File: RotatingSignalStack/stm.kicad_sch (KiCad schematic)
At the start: 16 parts, among them IC2 STM32H562RIT6, SW1 SW_Push, SW2 Boot Switch

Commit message: Minimal schematic
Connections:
- net STM_CLK_IN: now also IC2.5 (PH0-OSC_IN); no longer IC2.3 (PC14-OSC32_IN)
- no-connect marks 0 -> 29
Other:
- moved on the sheet: C13, C19, C20, C21, C30, C31, C32, C33, C34, C35

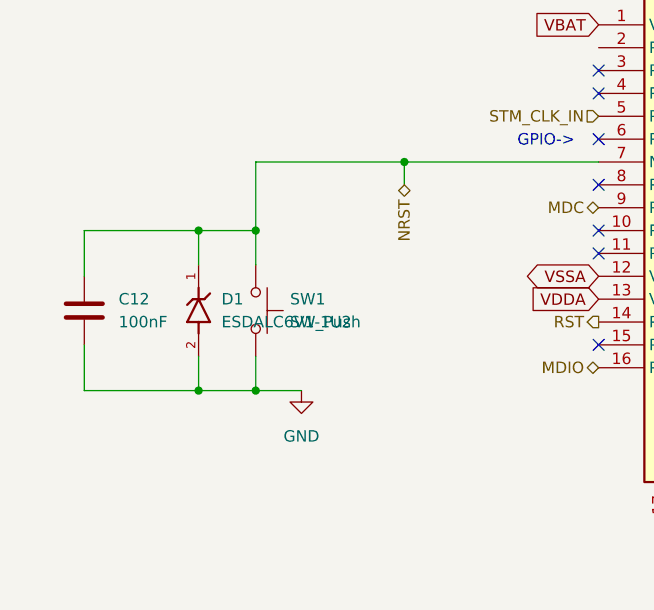
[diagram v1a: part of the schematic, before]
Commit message: Added ethernel ESD protection
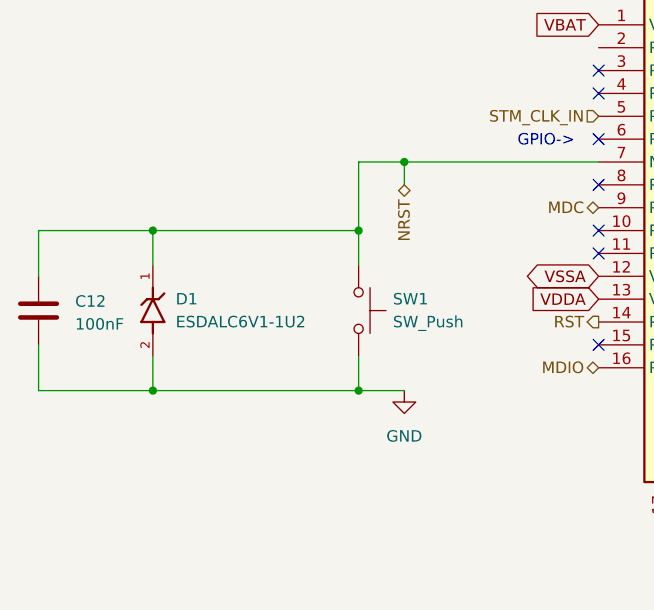
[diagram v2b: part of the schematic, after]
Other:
- moved on the sheet: C12, D1, SW1
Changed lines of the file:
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@@
 	)
 	(junction
-		(at 41.91 110.49)
+		(at 53.34 110.49)
 		(diameter 0)
 		(color 0 0 0 0)
 	)
 	(junction
-		(at 41.91 128.27)
+		(at 53.34 128.27)
 		(diameter 0)
 		(color 0 0 0 0)
@@
 	)
 	(junction
-		(at 35.56 110.49)
+		(at 30.48 110.49)
 		(diameter 0)
 		(color 0 0 0 0)
@@
 	)
 	(junction
-		(at 35.56 128.27)
+		(at 30.48 128.27)
 		(diameter 0)
 		(color 0 0 0 0)
@@
 	(wire
 		(pts
-			(xy 41.91 110.49) (xy 41.91 114.3)
+			(xy 53.34 110.49) (xy 53.34 114.3)
 		)
 		(stroke
@@
 	(wire
 		(pts
-			(xy 35.56 110.49) (xy 41.91 110.49)
+			(xy 30.48 110.49) (xy 53.34 110.49)
 		)
 		(stroke
@@
 	(wire
 		(pts
-			(xy 41.91 128.27) (xy 35.56 128.27)
+			(xy 53.34 128.27) (xy 30.48 128.27)
 		)
 		(stroke
@@
 	(wire
 		(pts
-			(xy 35.56 124.46) (xy 35.56 128.27)
+			(xy 30.48 124.46) (xy 30.48 128.27)
 		)
 		(stroke
@@
 	(wire
 		(pts
-			(xy 41.91 124.46) (xy 41.91 128.27)
+			(xy 53.34 124.46) (xy 53.34 128.27)
 		)
 		(stroke
@@
 	(wire
 		(pts
-			(xy 35.56 110.49) (xy 35.56 114.3)
+			(xy 30.48 110.49) (xy 30.48 114.3)
 		)
 		(stroke
@@
 	(wire
 		(pts
-			(xy 22.86 128.27) (xy 22.86 123.19)
-		)
-		(stroke
-			(width 0)
-			(type default)
-		)
-	)
-	(wire
-		(pts
 			(xy 58.42 102.87) (xy 58.42 105.41)
 		)
@@
 	(wire
 		(pts
-			(xy 22.86 115.57) (xy 22.86 110.49)
+			(xy 251.46 33.02) (xy 252.73 33.02)
 		)
 		(stroke
@@
 	(wire
 		(pts
-			(xy 35.56 128.27) (xy 22.86 128.27)
+			(xy 251.46 29.21) (xy 252.73 29.21)
 		)
 		(stroke
@@
 	(wire
 		(pts
-			(xy 251.46 33.02) (xy 252.73 33.02)
+			(xy 252.73 68.58) (xy 267.97 68.58)
 		)
 		(stroke
@@
 	(wire
 		(pts
-			(xy 251.46 29.21) (xy 252.73 29.21)
+			(xy 222.25 21.59) (xy 222.25 25.4)
 		)
 		(stroke
@@
 	(wire
 		(pts
-			(xy 252.73 68.58) (xy 267.97 68.58)
+			(xy 218.44 33.02) (xy 222.25 33.02)
 		)
 		(stroke
@@
 	(wire
 		(pts
-			(xy 222.25 21.59) (xy 222.25 25.4)
+			(xy 58.42 128.27) (xy 53.34 128.27)
 		)
 		(stroke
@@
 	(wire
 		(pts
-			(xy 22.86 110.49) (xy 35.56 110.49)
+			(xy 252.73 33.02) (xy 252.73 35.56)
 		)
 		(stroke
@@
 	(wire
 		(pts
-			(xy 218.44 33.02) (xy 222.25 33.02)
+			(xy 17.78 110.49) (xy 30.48 110.49)
 		)
 		(stroke
@@
 	(wire
 		(pts
-			(xy 46.99 128.27) (xy 41.91 128.27)
+			(xy 252.73 91.44) (xy 252.73 86.36)
 		)
 		(stroke
@@
 	(wire
 		(pts
-			(xy 252.73 33.02) (xy 252.73 35.56)
+			(xy 252.73 25.4) (xy 252.73 29.21)
 		)
 		(stroke
@@
 	(wire
 		(pts
-			(xy 252.73 91.44) (xy 252.73 86.36)
+			(xy 196.85 25.4) (xy 200.66 25.4)
 		)
 		(stroke
@@
 	(wire
 		(pts
-			(xy 252.73 25.4) (xy 252.73 29.21)
+			(xy 218.44 29.21) (xy 222.25 29.21)
 		)
 		(stroke
@@
 	(wire
 		(pts
-			(xy 196.85 25.4) (xy 200.66 25.4)
+			(xy 17.78 110.49) (xy 17.78 115.57)
 		)
 		(stroke
@@
 	(wire
 		(pts
-			(xy 218.44 29.21) (xy 222.25 29.21)
+			(xy 222.25 25.4) (xy 222.25 29.21)
 		)
 		(stroke
@@
 	(wire
 		(pts
-			(xy 222.25 25.4) (xy 222.25 29.21)
+			(xy 17.78 123.19) (xy 17.78 128.27)
 		)
 		(stroke
@@
 	(wire
 		(pts
-			(xy 41.91 102.87) (xy 41.91 110.49)
+			(xy 53.34 102.87) (xy 53.34 110.49)
+		)
+		(stroke
+			(width 0)
+			(type default)
+		)
+	)
+	(wire
+		(pts
+			(xy 17.78 128.27) (xy 30.48 128.27)
 		)
 		(stroke
@@
 	(wire
 		(pts
-			(xy 58.42 102.87) (xy 41.91 102.87)
+			(xy 53.34 102.87) (xy 58.42 102.87)
 		)
 		(stroke
@@
 	(symbol
 		(lib_id "Switch:SW_Push")
-		(at 41.91 119.38 270)
+		(at 53.34 119.38 270)
 		(unit 1)
 		(exclude_from_sim no)
@@
 		(fields_autoplaced yes)
 		(property "Reference" "SW1"
-			(at 45.72 118.1099 90)
+			(at 57.15 118.1099 90)
 			(effects
 				(font
@@
 		)
 		(property "Value" "SW_Push"
-			(at 45.72 120.6499 90)
+			(at 57.15 120.6499 90)
 			(effects
 				(font
@@
 		)
 		(property "Footprint" ""
-			(at 46.99 119.38 0)
+			(at 58.42 119.38 0)
 			(effects
 				(font
@@
 		)
 		(property "Datasheet" "~"
-			(at 46.99 119.38 0)
+			(at 58.42 119.38 0)
 			(effects
 				(font
@@
 		)
 		(property "Description" "Push button switch, generic, two pins"
-			(at 41.91 119.38 0)
+			(at 53.34 119.38 0)
 			(effects
 				(font
@@
 	(symbol
 		(lib_id "ESDALC6V1-1U2:ESDALC6V1-1U2")
-		(at 35.56 119.38 90)
+		(at 30.48 119.38 90)
 		(unit 1)
 		(exclude_from_sim no)
@@
 		(fields_autoplaced yes)
 		(property "Reference" "D1"
-			(at 38.1 118.1099 90)
+			(at 33.02 118.1099 90)
 			(effects
 				(font
@@
 		)
 		(property "Value" "ESDALC6V1-1U2"
-			(at 38.1 120.6499 90)
+			(at 33.02 120.6499 90)
 			(effects
 				(font
@@
 		)
 		(property "Footprint" "ESDALC6V1-1U2:DIODE_ESDALC6V1-1U2"
-			(at 35.56 119.38 0)
+			(at 30.48 119.38 0)
 			(effects
 				(font
@@
 		)
 		(property "Datasheet" ""
-			(at 35.56 119.38 0)
+			(at 30.48 119.38 0)
 			(effects
 				(font
@@
 		)
 		(property "Description" ""
-			(at 35.56 119.38 0)
+			(at 30.48 119.38 0)
 			(effects
 				(font
@@
 		)
 		(property "PARTREV" "3"
-			(at 35.56 119.38 0)
+			(at 30.48 119.38 0)
 			(effects
 				(font
@@
 		)
 		(property "STANDARD" "Manufacturer Recommendations"
-			(at 35.56 119.38 0)
+			(at 30.48 119.38 0)
 			(effects
 				(font
@@
 		)
 		(property "MAXIMUM_PACKAGE_HEIGHT" "0.33mm"
-			(at 35.56 119.38 0)
+			(at 30.48 119.38 0)
 			(effects
 				(font
@@
 		)
 		(property "MANUFACTURER" "STMicroelectronics"
-			(at 35.56 119.38 0)
+			(at 30.48 119.38 0)
 			(effects
 				(font
@@
 	(symbol
 		(lib_id "Device:C")
-		(at 22.86 119.38 0)
+		(at 17.78 119.38 0)
 		(unit 1)
 		(exclude_from_sim no)
@@
 		(on_board yes)
 		(dnp no)
-		(fields_autoplaced yes)
 		(property "Reference" "C12"
-			(at 26.67 118.1099 0)
+			(at 21.844 118.364 0)
 			(effects
 				(font
@@
 		)
 		(property "Value" "100nF"
-			(at 26.67 120.6499 0)
+			(at 21.844 120.904 0)
 			(effects
 				(font
@@
 		)
 		(property "Footprint" ""
-			(at 23.8252 123.19 0)
+			(at 18.7452 123.19 0)
 			(effects
 				(font
@@
 		)
 		(property "Datasheet" "~"
-			(at 22.86 119.38 0)
+			(at 17.78 119.38 0)
 			(effects
 				(font
@@
 		)
 		(property "Description" "Unpolarized capacitor"
-			(at 22.86 119.38 0)
+			(at 17.78 119.38 0)
 			(effects
 				(font
@@
 	(symbol
 		(lib_id "power:GND")
-		(at 46.99 128.27 0)
+		(at 58.42 128.27 0)
 		(unit 1)
 		(exclude_from_sim no)
@@
 		(fields_autoplaced yes)
 		(property "Reference" "#PWR034"
-			(at 46.99 134.62 0)
+			(at 58.42 134.62 0)
 			(effects
 				(font
@@
 		)
 		(property "Value" "GND"
-			(at 46.99 133.35 0)
+			(at 58.42 133.35 0)
 			(effects
 				(font
@@
 		)
 		(property "Footprint" ""
-			(at 46.99 128.27 0)
+			(at 58.42 128.27 0)
 			(effects
 				(font
@@
 		)
 		(property "Datasheet" ""
-			(at 46.99 128.27 0)
+			(at 58.42 128.27 0)
 			(effects
 				(font
@@
 		)
 		(property "Description" "Power symbol creates a global label with name \"GND\" , ground"
-			(at 46.99 128.27 0)
+			(at 58.42 128.27 0)
 			(effects
 				(font

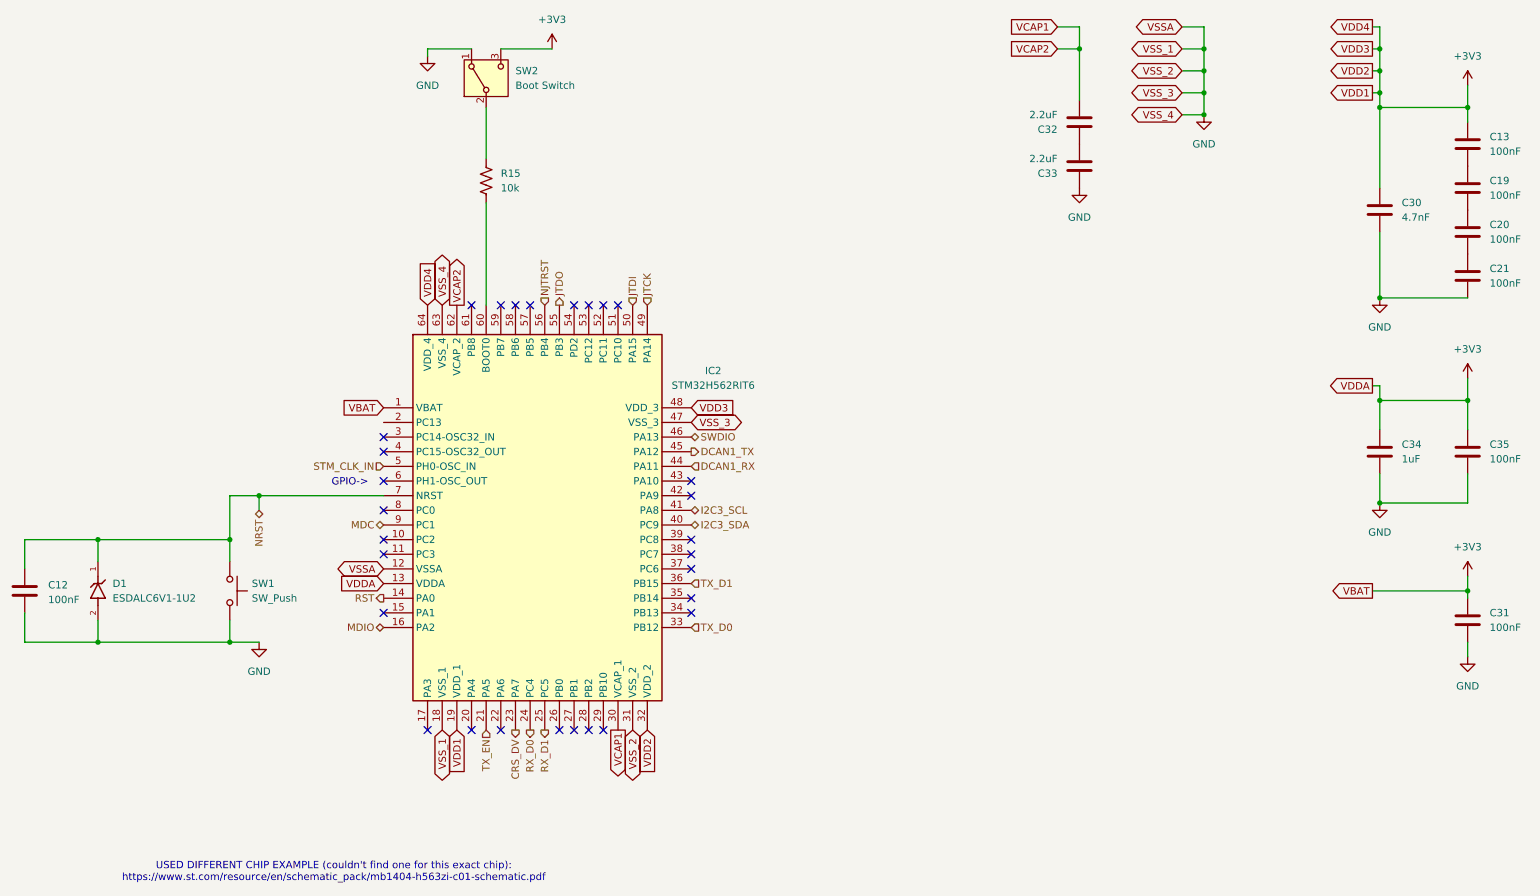
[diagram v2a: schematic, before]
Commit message: Added power LEDS
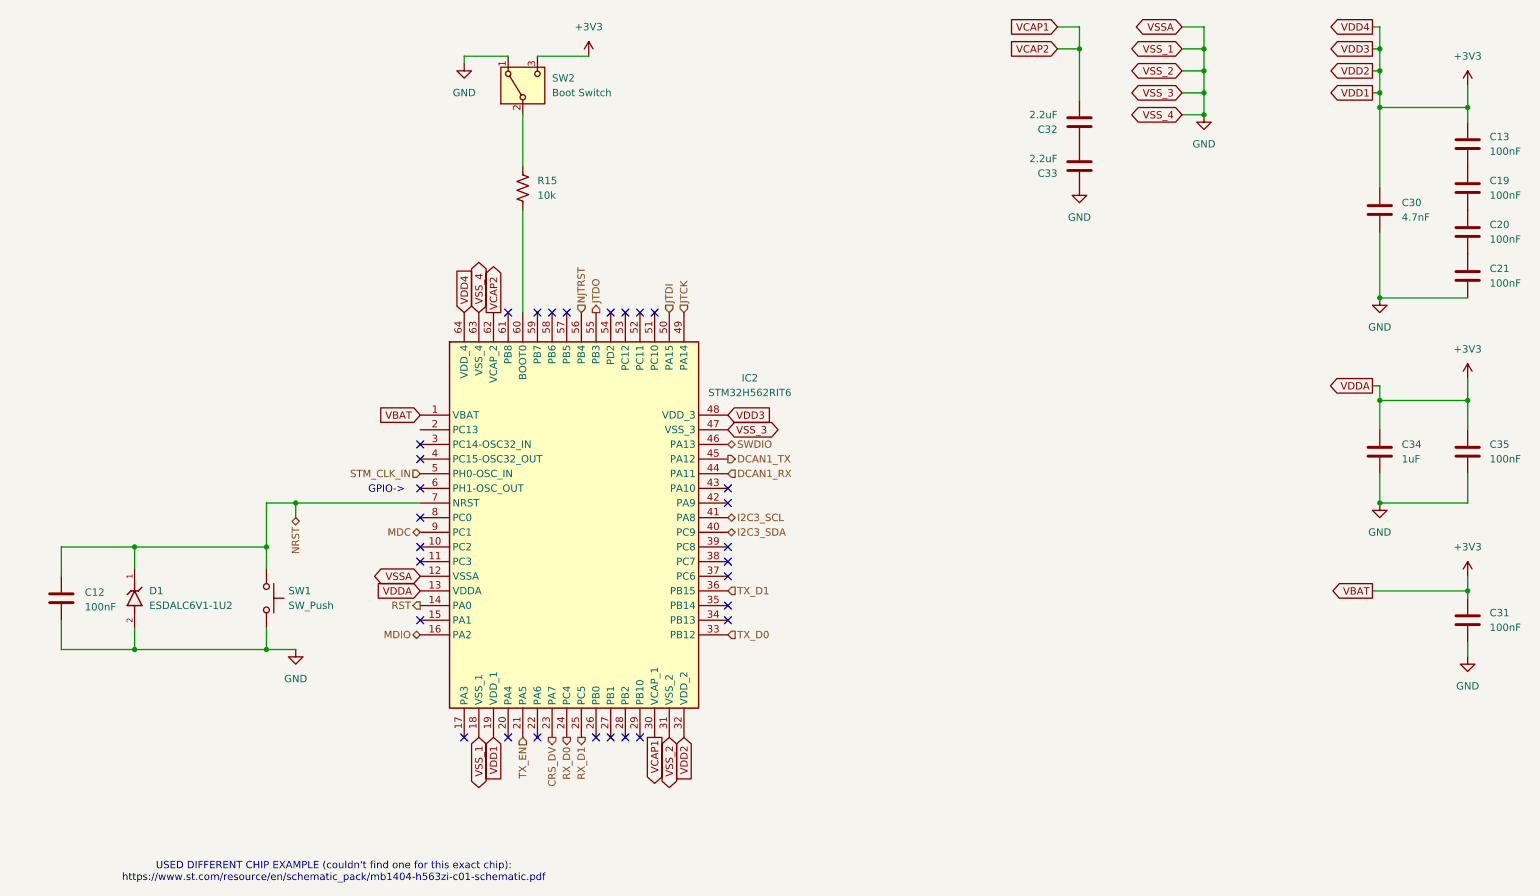
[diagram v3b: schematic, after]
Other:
- moved on the sheet: C12, D1, IC2, R15, SW1, SW2

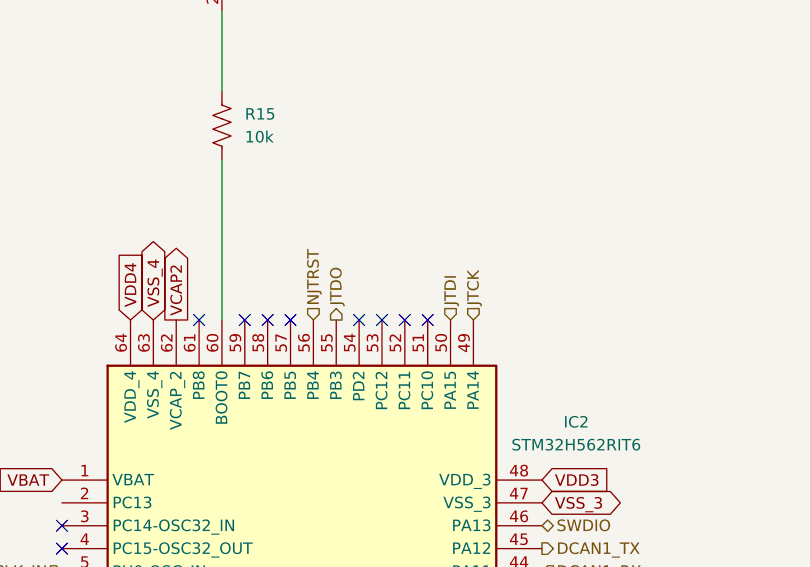
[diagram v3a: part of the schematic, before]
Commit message: Added buttons
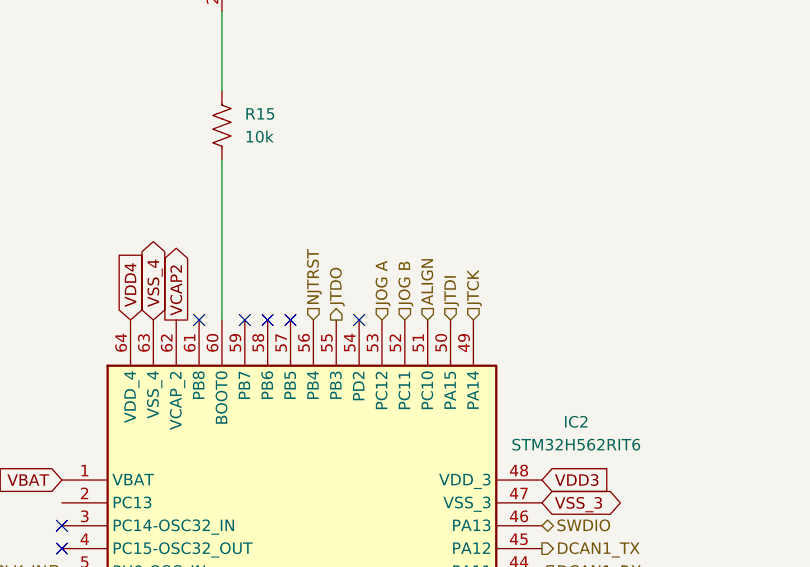
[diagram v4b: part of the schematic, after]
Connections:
- net ALIGN: now reaches IC2.51 (PC10)
- net JOG B: now reaches IC2.52 (PC11)
- net JOG A: now reaches IC2.53 (PC12)
- no-connect marks 29 -> 26
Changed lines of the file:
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@@
-	)
-	(no_connect
-		(at 127 71.12)
 	)
 	(no_connect
@@
 	)
 	(no_connect
-		(at 121.92 71.12)
-	)
-	(no_connect
 		(at 119.38 144.78)
 	)
@@
 	(no_connect
 		(at 139.7 101.6)
-	)
-	(no_connect
-		(at 124.46 71.12)
 	)
 	(no_connect
@@
 		)
 	)
+	(hierarchical_label "JOG B"
+		(shape input)
+		(at 124.46 71.12 90)
+		(effects
+			(font
+				(size 1.27 1.27)
+			)
+			(justify left)
+		)
+	)
 	(hierarchical_label "JTCK"
 		(shape input)
 		(at 132.08 71.12 90)
+		(effects
+			(font
+				(size 1.27 1.27)
+			)
+			(justify left)
+		)
+	)
+	(hierarchical_label "JOG A"
+		(shape input)
+		(at 121.92 71.12 90)
 		(effects
 			(font
@@
 		)
 	)
+	(hierarchical_label "ALIGN"
+		(shape input)
+		(at 127 71.12 90)
+		(effects
+			(font
+				(size 1.27 1.27)
+			)
+			(justify left)
+		)
+	)

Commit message: Added everything
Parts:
- C12, C13, C19, C20, C21, C30, C31, C32, C33, C34, C35: footprint (none) -> Capacitor_SMD:C_0603_1608Metric_Pad1.08x0.95mm_HandSolder
- D7: renamed from D1; footprint ESDALC6V1-1U2:DIODE_ESDALC6V1-1U2 -> SignalStack:DIODE_ESDALC6V1-1U2
- IC2: footprint QFP50P1200X1200X160-64N -> SignalStack:STM32H562RIT6
- R15: footprint (none) -> Resistor_SMD:R_0603_1608Metric_Pad0.98x0.95mm_HandSolder
- SW1: footprint (none) -> Button_Switch_SMD:SW_SPST_TL3305A
- SW2: footprint Button_Switch_THT:SW_Slide_SPDT_Angled_CK_OS102011MA1Q -> Button_Switch_THT:SW_Slide_SPDT_Straight_CK_OS102011MS2Q
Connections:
- net JTCK renamed SWCLK
- net JTDI: no longer names the net of IC2.50 (PA15)
- net JTDO renamed SWO
- net NJTRST: no longer names the net of IC2.56 (PB4)
- no-connect marks 26 -> 28
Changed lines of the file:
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@@
 	)
 	(no_connect
+		(at 114.3 71.12)
+	)
+	(no_connect
 		(at 86.36 96.52)
 	)
 	(no_connect
+		(at 129.54 71.12)
+	)
+	(no_connect
 		(at 86.36 93.98)
 	)
@@
 	(wire
 		(pts
+			(xy 222.25 39.37) (xy 222.25 36.83)
+		)
+		(stroke
+			(width 0)
+			(type default)
+		)
+	)
+	(wire
+		(pts
 			(xy 36.83 111.76) (xy 59.69 111.76)
 		)
@@
 	(wire
 		(pts
-			(xy 59.69 129.54) (xy 36.83 129.54)
+			(xy 36.83 129.54) (xy 59.69 129.54)
 		)
 		(stroke
@@
 		)
 	)
-	(hierarchical_label "JTDI"
-		(shape input)
-		(at 129.54 71.12 90)
-		(effects
-			(font
-				(size 1.27 1.27)
-			)
-			(justify left)
-		)
-	)
-	(hierarchical_label "JTDO"
+	(hierarchical_label "SWO"
 		(shape output)
 		(at 116.84 71.12 90)
@@
 		)
 	)
-	(hierarchical_label "JTCK"
+	(hierarchical_label "SWCLK"
 		(shape input)
 		(at 132.08 71.12 90)
@@
 		)
 	)
-	(hierarchical_label "NJTRST"
-		(shape input)
-		(at 114.3 71.12 90)
-		(effects
-			(font
-				(size 1.27 1.27)
-			)
-			(justify left)
-		)
-	)
 	(hierarchical_label "RX_D1"
 		(shape output)
@@
 			)
 		)
-		(property "Footprint" ""
+		(property "Footprint" "Button_Switch_SMD:SW_SPST_TL3305A"
 			(at 64.77 120.65 0)
 			(effects
@@
 			)
 		)
-		(property "Footprint" ""
+		(property "Footprint" "Capacitor_SMD:C_0603_1608Metric_Pad1.08x0.95mm_HandSolder"
 			(at 268.9352 53.34 0)
 			(effects
@@
 		(dnp no)
 		(fields_autoplaced yes)
-		(property "Reference" "D1"
+		(property "Reference" "D7"
 			(at 39.37 119.3799 90)
 			(effects
@@
 			)
 		)
-		(property "Footprint" "ESDALC6V1-1U2:DIODE_ESDALC6V1-1U2"
+		(property "Footprint" "SignalStack:DIODE_ESDALC6V1-1U2"
 			(at 36.83 120.65 0)
 			(effects
@@
 			(project ""
 				(path "/fbbbfa89-3c28-4cf8-856b-66ca7308742c/85f5c4be-2744-4dc6-8792-10e4391fb2cb"
-					(reference "D1")
+					(reference "D7")
 					(unit 1)
 				)
@@
 			)
 		)
-		(property "Footprint" ""
+		(property "Footprint" "Capacitor_SMD:C_0603_1608Metric_Pad1.08x0.95mm_HandSolder"
 			(at 253.6952 99.06 0)
 			(effects
@@
 			)
 		)
-		(property "Footprint" "QFP50P1200X1200X160-64N"
+		(property "Footprint" "SignalStack:STM32H562RIT6"
 			(at 135.89 173.66 0)
 			(effects
@@
 			)
 		)
-		(property "Footprint" ""
+		(property "Footprint" "Capacitor_SMD:C_0603_1608Metric_Pad1.08x0.95mm_HandSolder"
 			(at 268.9352 128.27 0)
 			(effects
@@
 			)
 		)
-		(property "Footprint" ""
+		(property "Footprint" "Capacitor_SMD:C_0603_1608Metric_Pad1.08x0.95mm_HandSolder"
 			(at 268.9352 99.06 0)
 			(effects
@@
 			)
 		)
-		(property "Footprint" ""
+		(property "Footprint" "Capacitor_SMD:C_0603_1608Metric_Pad1.08x0.95mm_HandSolder"
 			(at 268.9352 68.58 0)
 			(effects
@@
 			)
 		)
-		(property "Footprint" ""
+		(property "Footprint" "Capacitor_SMD:C_0603_1608Metric_Pad1.08x0.95mm_HandSolder"
 			(at 199.6948 34.29 0)
 			(effects
@@
 			)
 		)
-		(property "Footprint" "Button_Switch_THT:SW_Slide_SPDT_Angled_CK_OS102011MA1Q"
+		(property "Footprint" "Button_Switch_THT:SW_Slide_SPDT_Straight_CK_OS102011MS2Q"
 			(at 104.14 31.75 0)
 			(effects
@@
 			)
 		)
-		(property "Footprint" ""
+		(property "Footprint" "Capacitor_SMD:C_0603_1608Metric_Pad1.08x0.95mm_HandSolder"
 			(at 25.0952 124.46 0)
 			(effects
@@
 	(symbol
 		(lib_id "power:GND")
-		(at 222.25 36.83 0)
+		(at 222.25 39.37 0)
 		(unit 1)
 		(exclude_from_sim no)
@@
 		(fields_autoplaced yes)
 		(property "Reference" "#PWR010"
-			(at 222.25 43.18 0)
+			(at 222.25 45.72 0)
 			(effects
 				(font
@@
 		)
 		(property "Value" "GND"
-			(at 222.25 41.91 0)
+			(at 222.25 44.45 0)
 			(effects
 				(font
@@
 		)
 		(property "Footprint" ""
-			(at 222.25 36.83 0)
+			(at 222.25 39.37 0)
 			(effects
 				(font
@@
 		)
 		(property "Datasheet" ""
-			(at 222.25 36.83 0)
+			(at 222.25 39.37 0)
 			(effects
 				(font
@@
 		)
 		(property "Description" "Power symbol creates a global label with name \"GND\" , ground"
-			(at 222.25 36.83 0)
+			(at 222.25 39.37 0)
 			(effects
 				(font
@@
 			)
 		)
-		(property "Footprint" ""
+		(property "Footprint" "Capacitor_SMD:C_0603_1608Metric_Pad1.08x0.95mm_HandSolder"
 			(at 199.6948 41.91 0)
 			(effects
@@
 			)
 		)
-		(property "Footprint" ""
+		(property "Footprint" "Resistor_SMD:R_0603_1608Metric_Pad0.98x0.95mm_HandSolder"
 			(at 103.124 49.276 90)
 			(effects
@@
 			)
 		)
-		(property "Footprint" ""
+		(property "Footprint" "Capacitor_SMD:C_0603_1608Metric_Pad1.08x0.95mm_HandSolder"
 			(at 268.9352 45.72 0)
 			(effects
@@
 			)
 		)
-		(property "Footprint" ""
+		(property "Footprint" "Capacitor_SMD:C_0603_1608Metric_Pad1.08x0.95mm_HandSolder"
 			(at 253.6952 57.15 0)
 			(effects
@@
 			)
 		)
-		(property "Footprint" ""
+		(property "Footprint" "Capacitor_SMD:C_0603_1608Metric_Pad1.08x0.95mm_HandSolder"
 			(at 268.9352 60.96 0)
 			(effects
